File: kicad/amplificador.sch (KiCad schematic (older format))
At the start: 29 parts

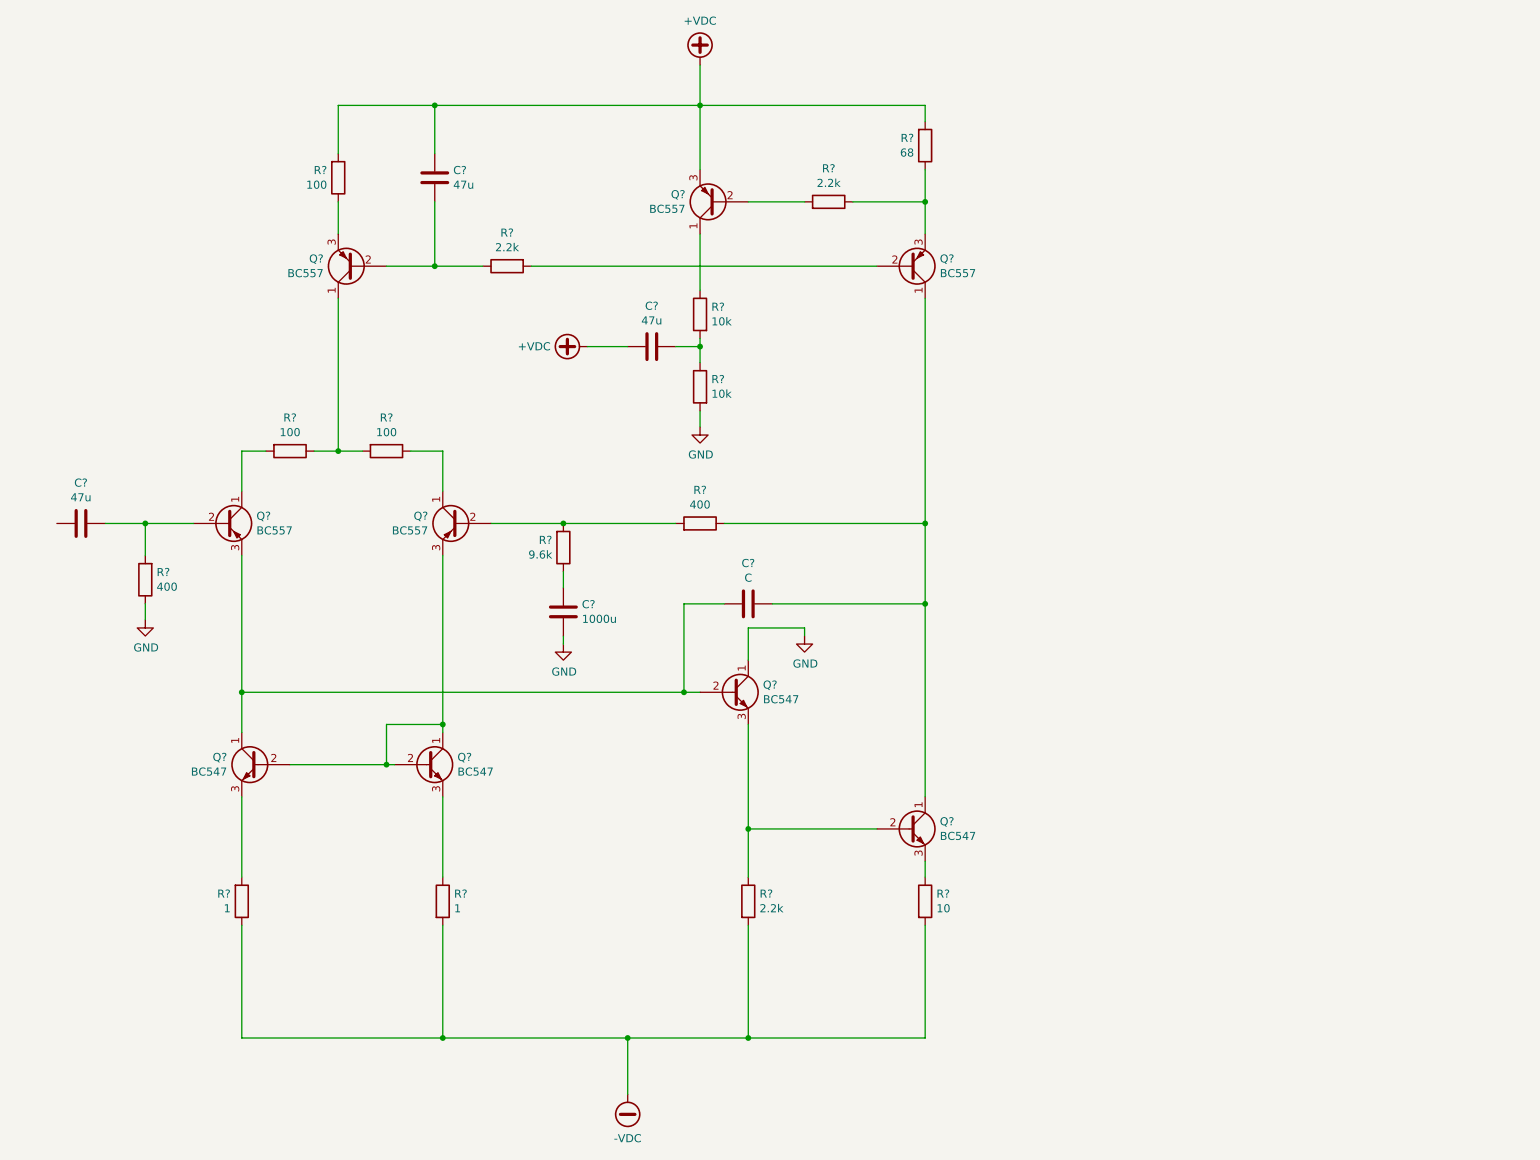
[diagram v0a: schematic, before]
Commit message: esquematico de kicad completo, faltan las fuentes interiores de la etapa de salida nada mas
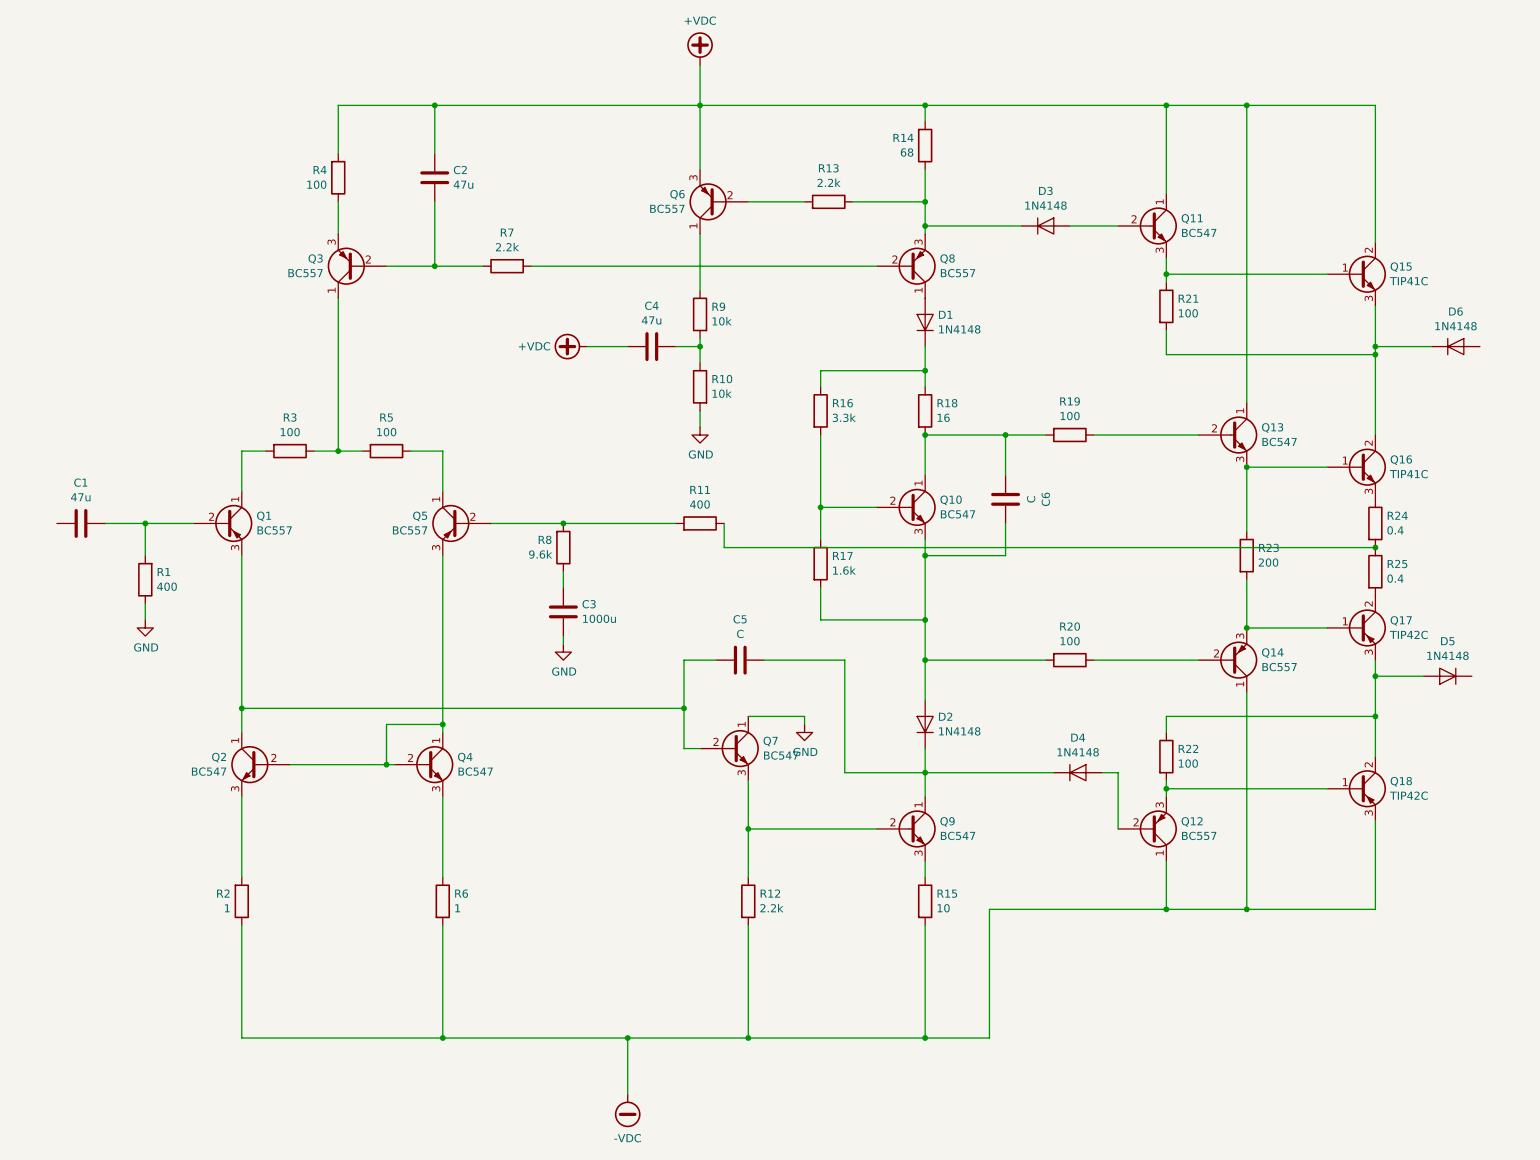
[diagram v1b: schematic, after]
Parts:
- added C6: C, symbol Device:C
- added D1, D2, D3, D4, D5, D6: 1N4148, Diode_THT:D_DO-35_SOD27_P7.62mm_Horizontal, symbol Diode:1N4148
- added Q10, Q11, Q13: BC547, Package_TO_SOT_THT:TO-92_Inline, symbol Transistor_BJT:BC547
- added Q12, Q14: BC557, Package_TO_SOT_THT:TO-92_Inline, symbol Transistor_BJT:BC557
- added Q15, Q16: TIP41C, Package_TO_SOT_THT:TO-220-3_Vertical, symbol Transistor_BJT:TIP41C
- added Q17, Q18: TIP42C, Package_TO_SOT_THT:TO-220-3_Vertical, symbol Transistor_BJT:TIP42C
- added R16: 3.3k, symbol Device:R
- added R17: 1.6k, symbol Device:R
- added R18: 16, symbol Device:R
- added R19, R20, R21, R22: 100, symbol Device:R
- added R23: 200, symbol Device:R
- added R24, R25: 0.4, symbol Device:R
- gave numbers to parts that had none: 29
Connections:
- net +VDC: now also Q11.1 (C), Q13.1 (C), Q15.2 (C)
- net -VDC: now also Q12.1 (C), Q14.1 (C), Q18.3 (E)
- net at Q8.3 (E), R13.1, R14.1: now also D3.1 (K)
- net at C5.1, Q9.1 (C): now also D2.1 (K), D4.1 (K); no longer Q8.1 (C), R11.1
- new net: R11.1, R24.2, R25.1
- new net: D1.2 (A), Q8.1 (C)
- new net: C6.2, Q10.1 (C), R18.2, R19.2
- new net: Q10.2 (B), R16.2, R17.1
- new net: C6.1, D2.2 (A), Q10.3 (E), R17.2, R20.2
- new net: D1.1 (K), R16.1, R18.1
- new net: Q14.2 (B), R20.1
- new net: Q13.2 (B), R19.1
- new net: D3.2 (A), Q11.2 (B)
- new net: Q11.3 (E), Q15.1 (B), R21.1
- new net: Q13.3 (E), Q16.1 (B), R23.1
- new net: Q14.3 (E), Q17.1 (B), R23.2
- new net: D4.2 (A), Q12.2 (B)
- new net: Q12.3 (E), Q18.1 (B), R22.2
- new net: D5.2 (A), Q17.3 (E), Q18.2 (C), R22.1
- new net: D6.1 (K), Q15.3 (E), Q16.2 (C), R21.2
- new net: Q16.3 (E), R24.1
- new net: Q17.2 (C), R25.2
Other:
- moved on the sheet: C5, Q7

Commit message: Seleccionado de footprints para resistores smd
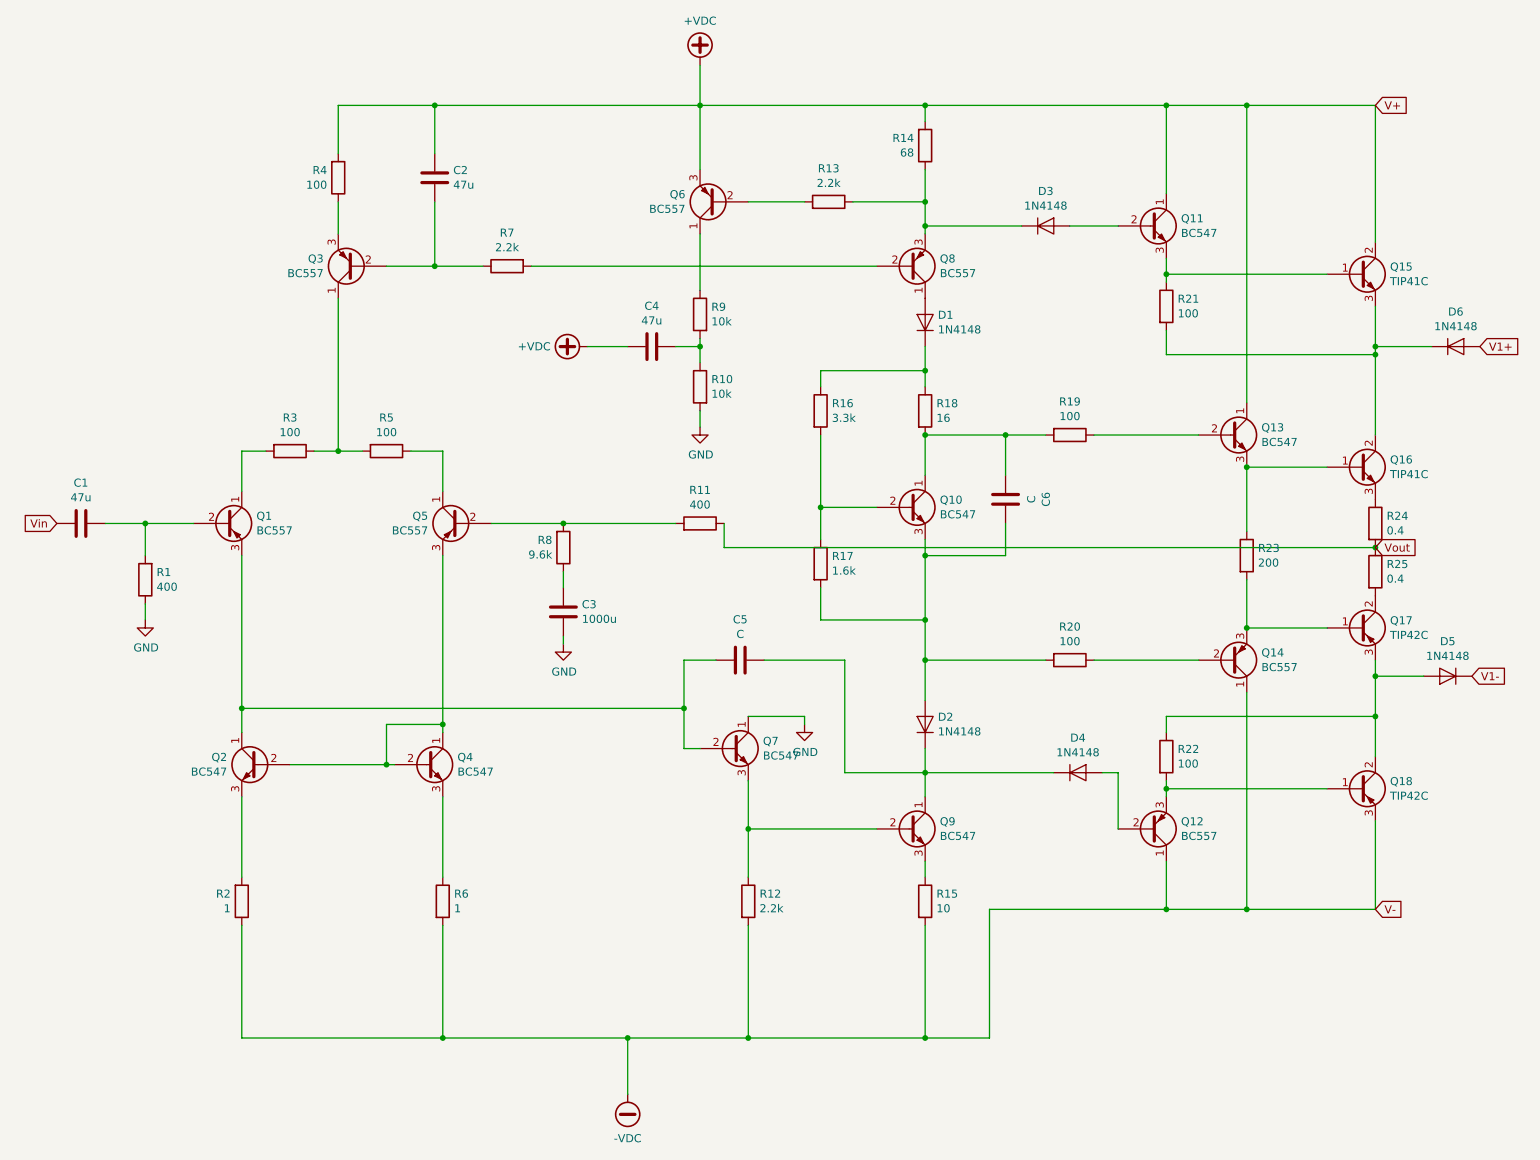
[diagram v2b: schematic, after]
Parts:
- R1, R10, R11, R12, R13, R14, R15, R16, R17, R18, R19, R2, R20, R21, R22, R23, R24, R25, R3, R4, R5, R6, R7, R8, R9: footprint (none) -> Resistor_SMD:R_0805_2012Metric_Pad1.15x1.40mm_HandSolder
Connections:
- net Vout: now reaches R11.1, R24.2, R25.1
- net Vin: now reaches C1.2
- net V1+: now reaches D6.2 (A)
- net V1-: now reaches D5.1 (K)
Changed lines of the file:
@@
 F 0 "R3" V 2293 3400 50  0000 C CNN
 F 1 "100" V 2384 3400 50  0000 C CNN
-F 2 "" V 2430 3400 50  0001 C CNN
+F 2 "Resistor_SMD:R_0805_2012Metric_Pad1.15x1.40mm_HandSolder" V 2430 3400 50  0001 C CNN
 F 3 "~" H 2500 3400 50  0001 C CNN
 	1    2500 3400
@@
 F 0 "R5" V 2893 3400 50  0000 C CNN
 F 1 "100" V 2984 3400 50  0000 C CNN
-F 2 "" V 3030 3400 50  0001 C CNN
+F 2 "Resistor_SMD:R_0805_2012Metric_Pad1.15x1.40mm_HandSolder" V 3030 3400 50  0001 C CNN
 F 3 "~" H 3100 3400 50  0001 C CNN
 	1    3100 3400
@@
 F 0 "R2" H 2131 6154 50  0000 R CNN
 F 1 "1" H 2131 6245 50  0000 R CNN
-F 2 "" V 2130 6200 50  0001 C CNN
+F 2 "Resistor_SMD:R_0805_2012Metric_Pad1.15x1.40mm_HandSolder" V 2130 6200 50  0001 C CNN
 F 3 "~" H 2200 6200 50  0001 C CNN
 	1    2200 6200
@@
 F 0 "R6" H 3520 6246 50  0000 L CNN
 F 1 "1" H 3520 6155 50  0000 L CNN
-F 2 "" V 3380 6200 50  0001 C CNN
+F 2 "Resistor_SMD:R_0805_2012Metric_Pad1.15x1.40mm_HandSolder" V 3380 6200 50  0001 C CNN
 F 3 "~" H 3450 6200 50  0001 C CNN
 	1    3450 6200
@@
 F 0 "R4" H 2731 1654 50  0000 R CNN
 F 1 "100" H 2731 1745 50  0000 R CNN
-F 2 "" V 2730 1700 50  0001 C CNN
+F 2 "Resistor_SMD:R_0805_2012Metric_Pad1.15x1.40mm_HandSolder" V 2730 1700 50  0001 C CNN
 F 3 "~" H 2800 1700 50  0001 C CNN
 	1    2800 1700
@@
 F 0 "R7" V 3643 2250 50  0000 C CNN
 F 1 "2.2k" V 3734 2250 50  0000 C CNN
-F 2 "" V 3780 2250 50  0001 C CNN
+F 2 "Resistor_SMD:R_0805_2012Metric_Pad1.15x1.40mm_HandSolder" V 3780 2250 50  0001 C CNN
 F 3 "~" H 3850 2250 50  0001 C CNN
 	1    3850 2250
@@
 F 0 "R9" H 4980 2596 50  0000 R CNN
 F 1 "10k" H 4980 2505 50  0000 R CNN
-F 2 "" V 4980 2550 50  0001 C CNN
+F 2 "Resistor_SMD:R_0805_2012Metric_Pad1.15x1.40mm_HandSolder" V 4980 2550 50  0001 C CNN
 F 3 "~" H 5050 2550 50  0001 C CNN
 	1    5050 2550
@@
 F 0 "R10" H 4980 3046 50  0000 R CNN
 F 1 "10k" H 4980 2955 50  0000 R CNN
-F 2 "" V 4980 3000 50  0001 C CNN
+F 2 "Resistor_SMD:R_0805_2012Metric_Pad1.15x1.40mm_HandSolder" V 4980 3000 50  0001 C CNN
 F 3 "~" H 5050 3000 50  0001 C CNN
 	1    5050 3000
@@
 F 0 "R13" V 6057 1850 50  0000 C CNN
 F 1 "2.2k" V 5966 1850 50  0000 C CNN
-F 2 "" V 5780 1850 50  0001 C CNN
+F 2 "Resistor_SMD:R_0805_2012Metric_Pad1.15x1.40mm_HandSolder" V 5780 1850 50  0001 C CNN
 F 3 "~" H 5850 1850 50  0001 C CNN
 	1    5850 1850
@@
 F 0 "R14" H 6381 1454 50  0000 R CNN
 F 1 "68" H 6381 1545 50  0000 R CNN
-F 2 "" V 6380 1500 50  0001 C CNN
+F 2 "Resistor_SMD:R_0805_2012Metric_Pad1.15x1.40mm_HandSolder" V 6380 1500 50  0001 C CNN
 F 3 "~" H 6450 1500 50  0001 C CNN
 	1    6450 1500
@@
 F 0 "R11" V 5257 3850 50  0000 C CNN
 F 1 "400" V 5166 3850 50  0000 C CNN
-F 2 "" V 4980 3850 50  0001 C CNN
+F 2 "Resistor_SMD:R_0805_2012Metric_Pad1.15x1.40mm_HandSolder" V 4980 3850 50  0001 C CNN
 F 3 "~" H 5050 3850 50  0001 C CNN
 	1    5050 3850
@@
 F 0 "R8" H 4131 3954 50  0000 R CNN
 F 1 "9.6k" H 4131 4045 50  0000 R CNN
-F 2 "" V 4130 4000 50  0001 C CNN
+F 2 "Resistor_SMD:R_0805_2012Metric_Pad1.15x1.40mm_HandSolder" V 4130 4000 50  0001 C CNN
 F 3 "~" H 4200 4000 50  0001 C CNN
 	1    4200 4000
@@
 F 0 "R12" H 5420 6246 50  0000 L CNN
 F 1 "2.2k" H 5420 6155 50  0000 L CNN
-F 2 "" V 5280 6200 50  0001 C CNN
+F 2 "Resistor_SMD:R_0805_2012Metric_Pad1.15x1.40mm_HandSolder" V 5280 6200 50  0001 C CNN
 F 3 "~" H 5350 6200 50  0001 C CNN
 	1    5350 6200
@@
 F 0 "R15" H 6520 6246 50  0000 L CNN
 F 1 "10" H 6520 6155 50  0000 L CNN
-F 2 "" V 6380 6200 50  0001 C CNN
+F 2 "Resistor_SMD:R_0805_2012Metric_Pad1.15x1.40mm_HandSolder" V 6380 6200 50  0001 C CNN
 F 3 "~" H 6450 6200 50  0001 C CNN
 	1    6450 6200
@@
 F 0 "R1" H 1530 4154 50  0000 R CNN
 F 1 "400" H 1530 4245 50  0000 R CNN
-F 2 "" V 1530 4200 50  0001 C CNN
+F 2 "Resistor_SMD:R_0805_2012Metric_Pad1.15x1.40mm_HandSolder" V 1530 4200 50  0001 C CNN
 F 3 "~" H 1600 4200 50  0001 C CNN
 	1    1600 4200
@@
 F 0 "R18" H 6520 3196 50  0000 L CNN
 F 1 "16" H 6520 3105 50  0000 L CNN
-F 2 "" V 6380 3150 50  0001 C CNN
+F 2 "Resistor_SMD:R_0805_2012Metric_Pad1.15x1.40mm_HandSolder" V 6380 3150 50  0001 C CNN
 F 3 "~" H 6450 3150 50  0001 C CNN
 	1    6450 3150
@@
 F 0 "R16" H 5870 3196 50  0000 L CNN
 F 1 "3.3k" H 5870 3105 50  0000 L CNN
-F 2 "" V 5730 3150 50  0001 C CNN
+F 2 "Resistor_SMD:R_0805_2012Metric_Pad1.15x1.40mm_HandSolder" V 5730 3150 50  0001 C CNN
 F 3 "~" H 5800 3150 50  0001 C CNN
 	1    5800 3150
@@
 F 0 "R17" H 5870 4146 50  0000 L CNN
 F 1 "1.6k" H 5870 4055 50  0000 L CNN
-F 2 "" V 5730 4100 50  0001 C CNN
+F 2 "Resistor_SMD:R_0805_2012Metric_Pad1.15x1.40mm_HandSolder" V 5730 4100 50  0001 C CNN
 F 3 "~" H 5800 4100 50  0001 C CNN
 	1    5800 4100
@@
 F 0 "R20" V 7143 4700 50  0000 C CNN
 F 1 "100" V 7234 4700 50  0000 C CNN
-F 2 "" V 7280 4700 50  0001 C CNN
+F 2 "Resistor_SMD:R_0805_2012Metric_Pad1.15x1.40mm_HandSolder" V 7280 4700 50  0001 C CNN
 F 3 "~" H 7350 4700 50  0001 C CNN
 	1    7350 4700
@@
 F 0 "R19" V 7143 3300 50  0000 C CNN
 F 1 "100" V 7234 3300 50  0000 C CNN
-F 2 "" V 7280 3300 50  0001 C CNN
+F 2 "Resistor_SMD:R_0805_2012Metric_Pad1.15x1.40mm_HandSolder" V 7280 3300 50  0001 C CNN
 F 3 "~" H 7350 3300 50  0001 C CNN
 	1    7350 3300
@@
 F 0 "R23" H 8520 4096 50  0000 L CNN
 F 1 "200" H 8520 4005 50  0000 L CNN
-F 2 "" V 8380 4050 50  0001 C CNN
+F 2 "Resistor_SMD:R_0805_2012Metric_Pad1.15x1.40mm_HandSolder" V 8380 4050 50  0001 C CNN
 F 3 "~" H 8450 4050 50  0001 C CNN
 	1    8450 4050
@@
 F 0 "R22" H 8020 5346 50  0000 L CNN
 F 1 "100" H 8020 5255 50  0000 L CNN
-F 2 "" V 7880 5300 50  0001 C CNN
+F 2 "Resistor_SMD:R_0805_2012Metric_Pad1.15x1.40mm_HandSolder" V 7880 5300 50  0001 C CNN
 F 3 "~" H 7950 5300 50  0001 C CNN
 	1    7950 5300
@@
 F 0 "R21" H 8020 2546 50  0000 L CNN
 F 1 "100" H 8020 2455 50  0000 L CNN
-F 2 "" V 7880 2500 50  0001 C CNN
+F 2 "Resistor_SMD:R_0805_2012Metric_Pad1.15x1.40mm_HandSolder" V 7880 2500 50  0001 C CNN
 F 3 "~" H 7950 2500 50  0001 C CNN
 	1    7950 2500
@@
 F 0 "R25" H 9320 4196 50  0000 L CNN
 F 1 "0.4" H 9320 4105 50  0000 L CNN
-F 2 "" V 9180 4150 50  0001 C CNN
+F 2 "Resistor_SMD:R_0805_2012Metric_Pad1.15x1.40mm_HandSolder" V 9180 4150 50  0001 C CNN
 F 3 "~" H 9250 4150 50  0001 C CNN
 	1    9250 4150
@@
 F 0 "R24" H 9320 3896 50  0000 L CNN
 F 1 "0.4" H 9320 3805 50  0000 L CNN
-F 2 "" V 9180 3850 50  0001 C CNN
+F 2 "Resistor_SMD:R_0805_2012Metric_Pad1.15x1.40mm_HandSolder" V 9180 3850 50  0001 C CNN
 F 3 "~" H 9250 3850 50  0001 C CNN
 	1    9250 3850
@@
 	-1   0    0    1
 $EndComp
+Text GLabel 1050 3850 0    50   Input ~ 0
+Vin
+Text GLabel 9850 4800 2    50   Input ~ 0
+V1-
+Text GLabel 9900 2750 2    50   Input ~ 0
+V1+
+Text GLabel 9250 1250 2    50   Input ~ 0
+V+
+Text GLabel 9250 6250 2    50   Input ~ 0
+V-
+Text GLabel 9250 4000 2    50   Input ~ 0
+Vout
 $EndSCHEMATC
